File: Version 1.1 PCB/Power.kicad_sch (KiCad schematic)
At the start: 19 parts

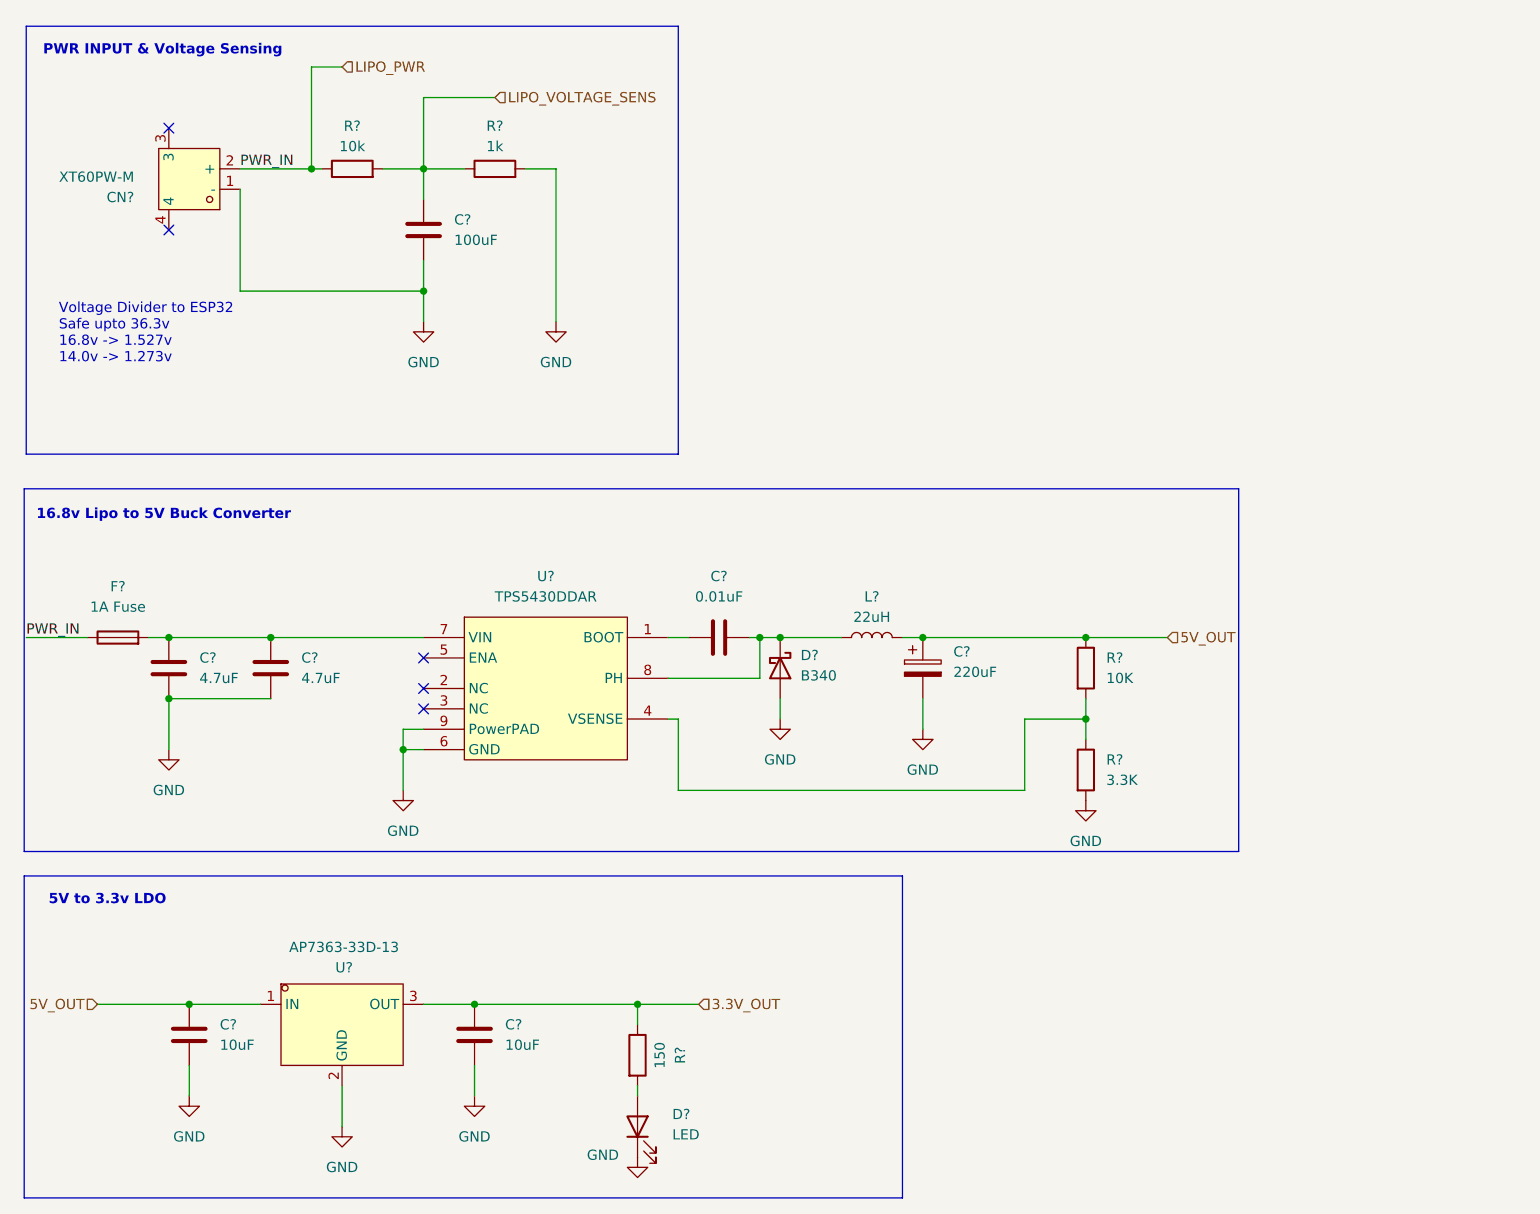
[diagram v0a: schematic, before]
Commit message: Added pins
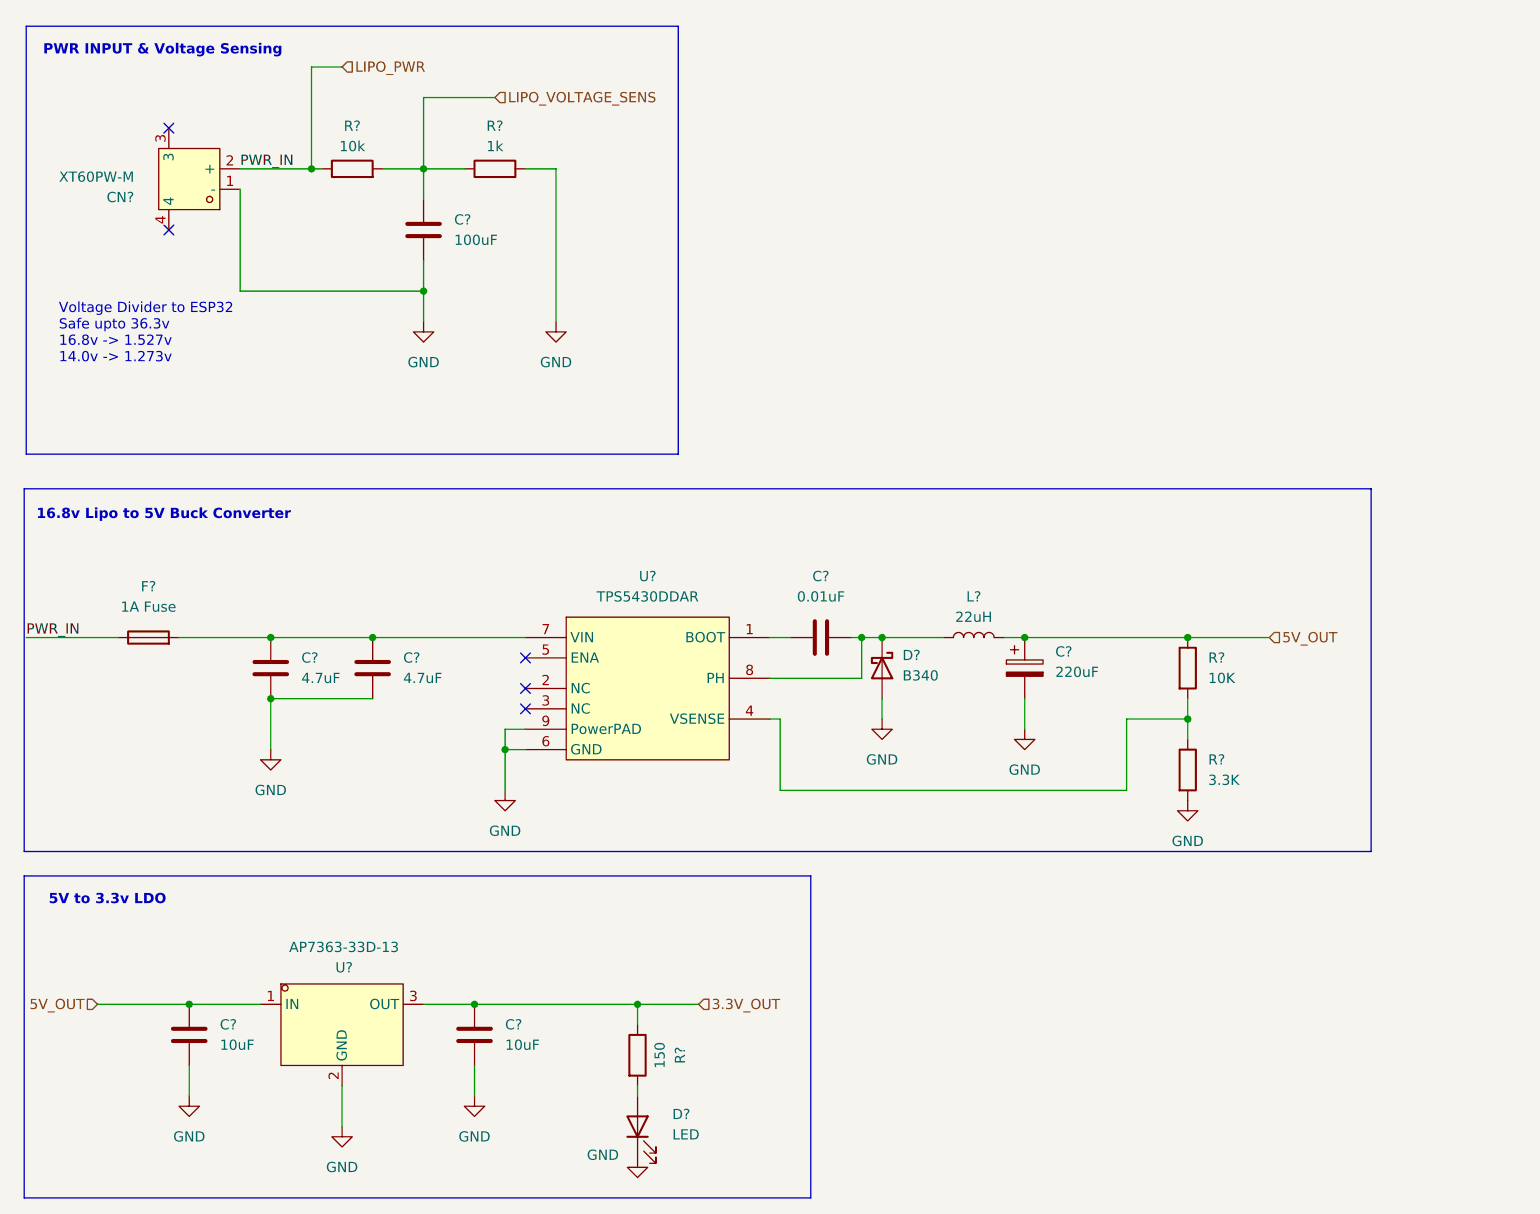
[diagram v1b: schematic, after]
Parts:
- F?: footprint (none) -> Fuse:Fuse_1206_3216Metric_Pad1.42x1.75mm_HandSolder
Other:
- moved on the sheet: C?, D?, F?, L?, R?, U?

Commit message: Added soft starter to PCB
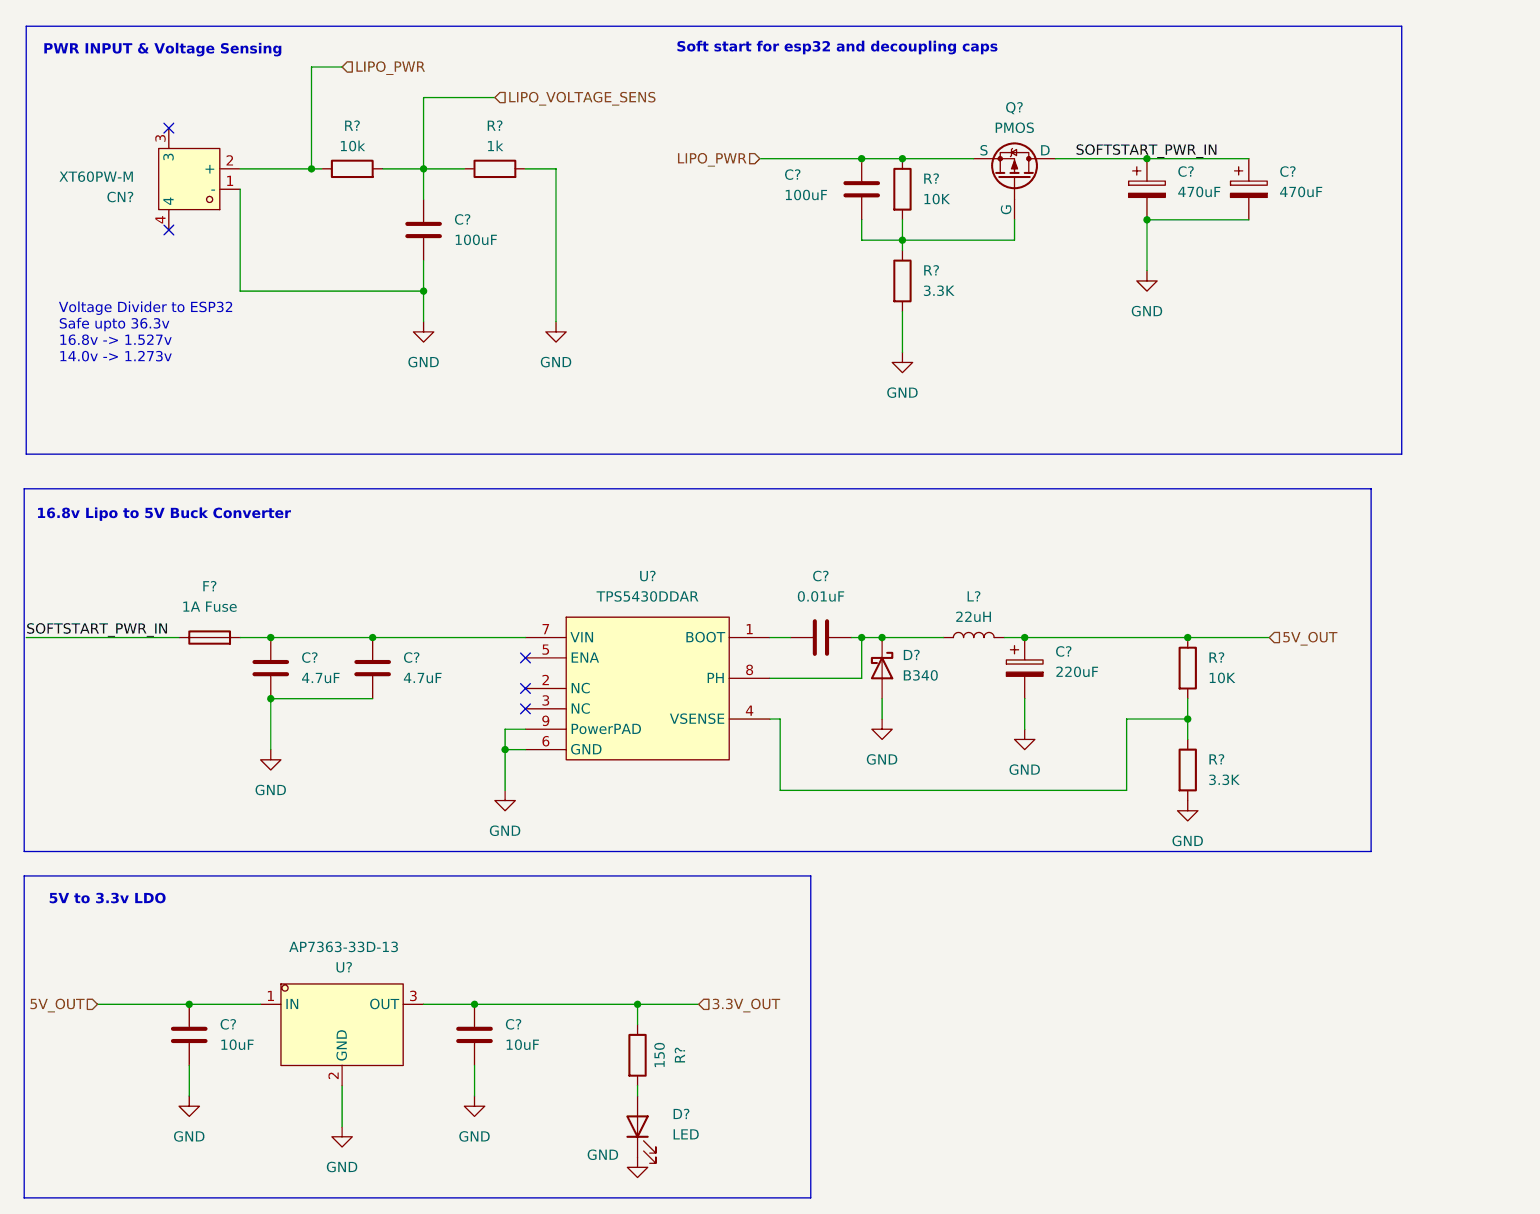
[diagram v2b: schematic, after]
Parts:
- added C? (x2): 470uF, symbol Device:C_Polarized
- added C?: 100uF, symbol Device:C
- added Q?: PMOS, symbol Simulation_SPICE:PMOS
- added R?: 10K, symbol Device:R
- added R?: 3.3K, symbol Device:R
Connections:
- net GND: now also C?.2, C?.2, R?.2
- net LIPO_PWR: now also C?.2, Q?.3 (S), R?.1; no longer F?.1
- new net: C?.1, Q?.2 (G), R?.1, R?.2
- new net SOFTSTART_PWR_IN: C?.1, C?.1, F?.1, Q?.1 (D)
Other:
- note added: "Soft start for esp32 and decoupling caps"
- moved on the sheet: F?

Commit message: Added ESD protection and test pins
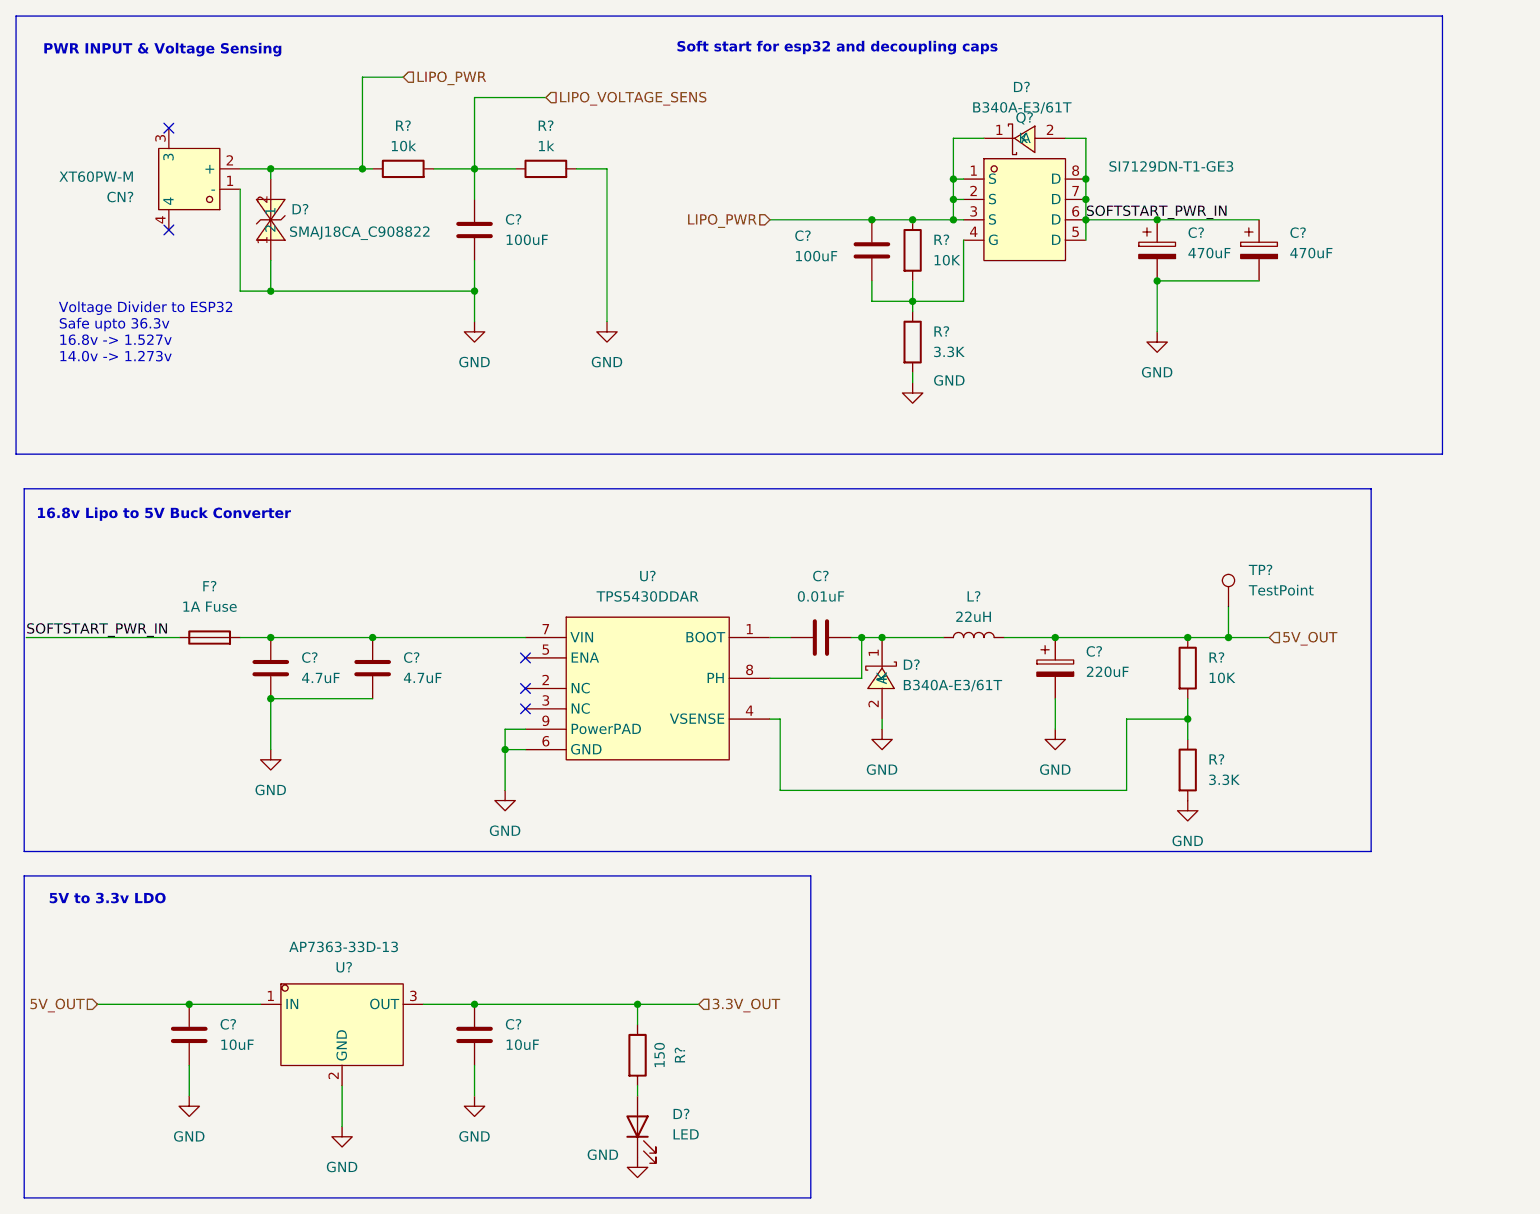
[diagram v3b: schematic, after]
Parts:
- removed D?: B340, Diode_SMD:D_SMC, symbol Diode:B340
- removed Q?: PMOS, symbol Simulation_SPICE:PMOS
- added D? (x2): B340A-E3/61T, easyeda2kicad:SMA_L4.3-W2.6-LS5.2-RD, symbol easyeda2kicad:B340A-E3_61T
- added D?: SMAJ18CA_C908822, easyeda2kicad:SMA_L4.4-W2.8-LS5.1-BI, symbol easyeda2kicad:SMAJ18CA_C908822
- added Q?: SI7129DN-T1-GE3, easyeda2kicad:POWERPAK-1212-8_L3.3-W3.3-P0.65-BL-EP, symbol easyeda2kicad:SI7129DN-T1-GE3
- added TP?: TestPoint, TestPoint:TestPoint_Pad_D3.0mm, symbol Connector:TestPoint
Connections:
- net 5V_OUT: now also TP?.1
- net GND: now also D?.1, D?.2 (A)
- net LIPO_PWR: now also D?.1 (K), D?.2, Q?.1 (S), Q?.2 (S), Q?.3 (S)
- net SOFTSTART_PWR_IN: now also D?.2 (A), Q?.5 (D), Q?.6 (D), Q?.7 (D), Q?.8 (D)
- net at C?.2, L?.1, U?.8 (PH): now also D?.1 (K)
- net at C?.1, R?.1, R?.2: now also Q?.4 (G)
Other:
- moved on the sheet: C?, R?

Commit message: began part placement
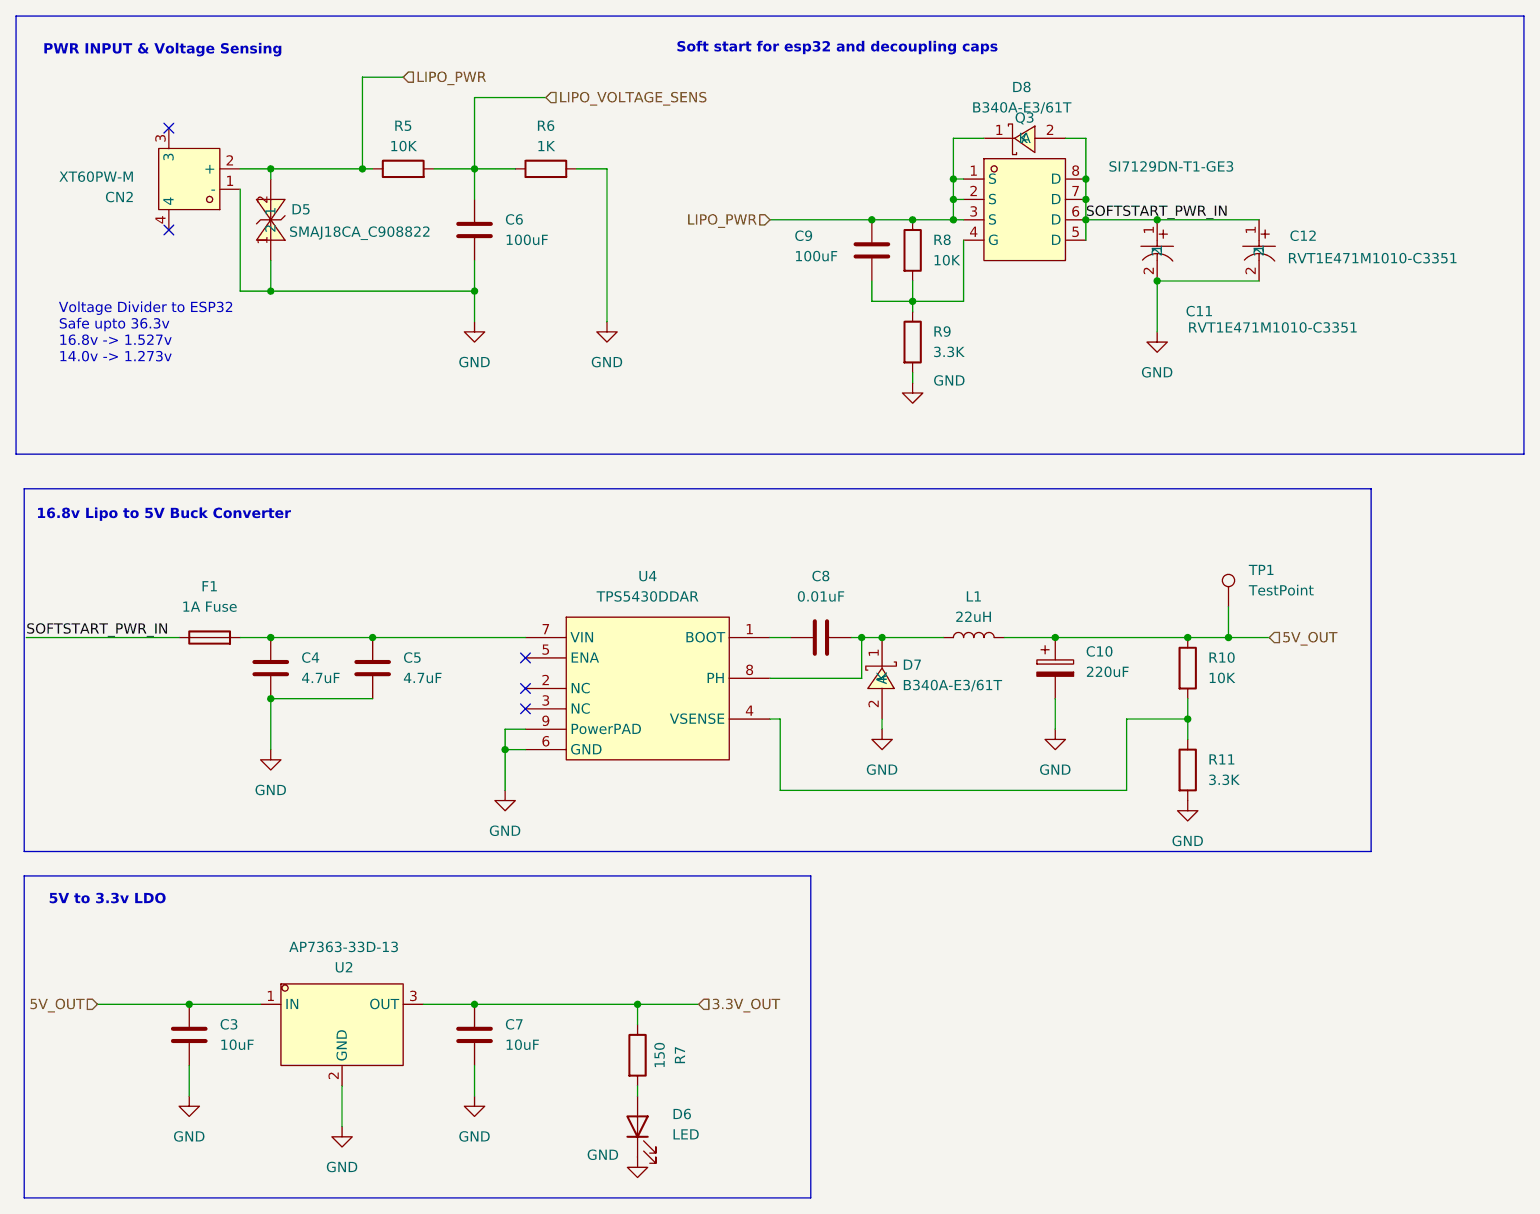
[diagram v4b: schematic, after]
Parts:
- removed C? (x2): 470uF, symbol Device:C_Polarized
- added C11, C12: RVT1E471M1010-C3351, easyeda2kicad:CAP-SMD_BD10.0-L10.3-W10.3-LS11.0-FD, symbol easyeda2kicad:RVT1E471M1010-C3351
- C10, C3, C4, C5, C6, C7, C8, C9: renamed from C?; footprint (none) -> Capacitor_SMD:C_0805_2012Metric_Pad1.18x1.45mm_HandSolder
- D6: renamed from D?; footprint (none) -> LED_SMD:LED_0805_2012Metric_Pad1.15x1.40mm_HandSolder
- L1: renamed from L?; footprint (none) -> easyeda2kicad:IND-SMD_L5.5-W5.2
- R10, R11, R7, R8, R9: renamed from R?; footprint (none) -> Resistor_SMD:R_0805_2012Metric_Pad1.20x1.40mm_HandSolder
- R5: renamed from R?; value 10k -> 10K; footprint (none) -> Resistor_SMD:R_0805_2012Metric_Pad1.20x1.40mm_HandSolder
- R6: renamed from R?; value 1k -> 1K; footprint (none) -> Resistor_SMD:R_0805_2012Metric_Pad1.20x1.40mm_HandSolder
- gave numbers to parts that had none: 9
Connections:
- net GND: now also C11.2, C12.2
- net SOFTSTART_PWR_IN: now also C11.1, C12.1
